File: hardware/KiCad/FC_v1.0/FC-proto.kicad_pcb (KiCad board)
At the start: 4 copper layers, 56 x 46 mm, 134 parts, among them J1 SM06B-GHS-TB, J10 PAD_OUT, J11 PAD_OUT, J12 PAD_OUT_Mini, J13 PAD_OUT_Mini, J2 MEM2061-01-188-00-A, J3 USB4105-GF-A, J4 Conn_ARM_SWD_TagConnect_TC203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, J5 SM06B-GHS-TB, J6 SM04B-GHS-TB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

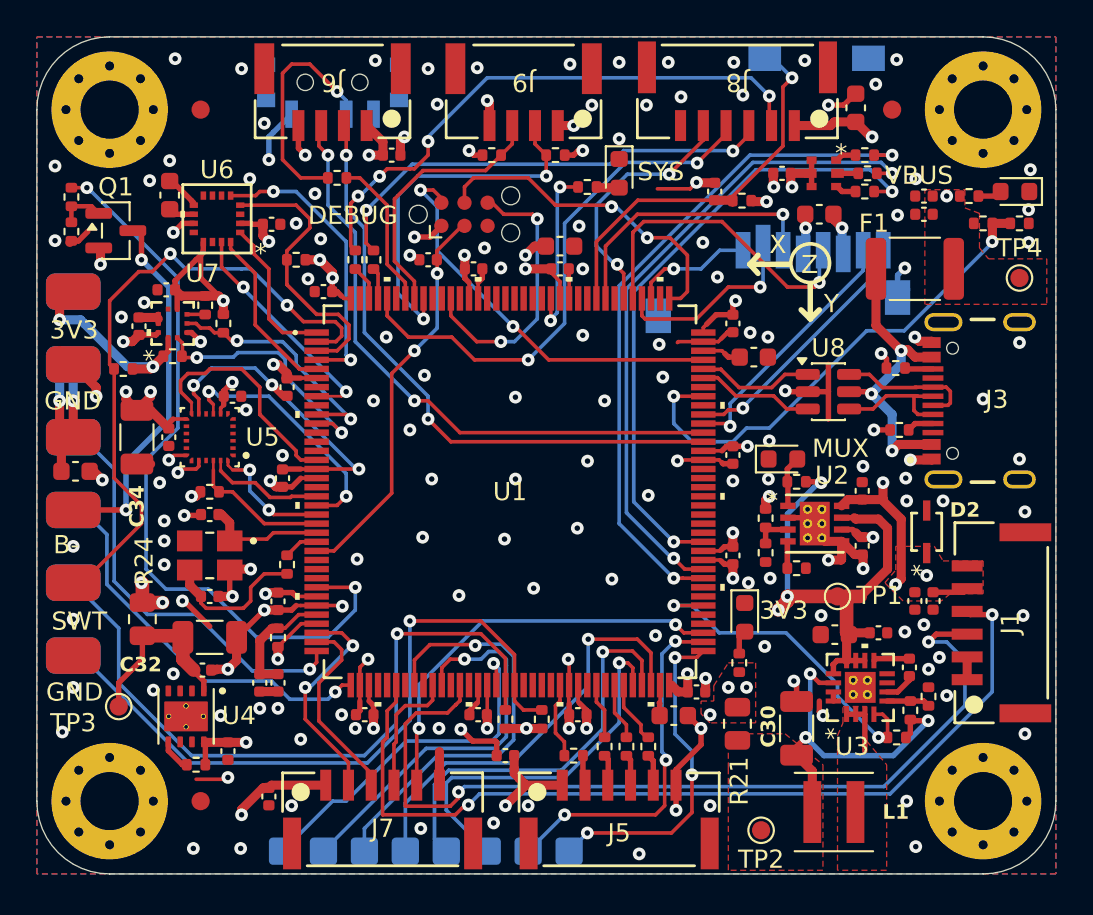
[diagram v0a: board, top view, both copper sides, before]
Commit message: changing USB ESD IC (v0.8)
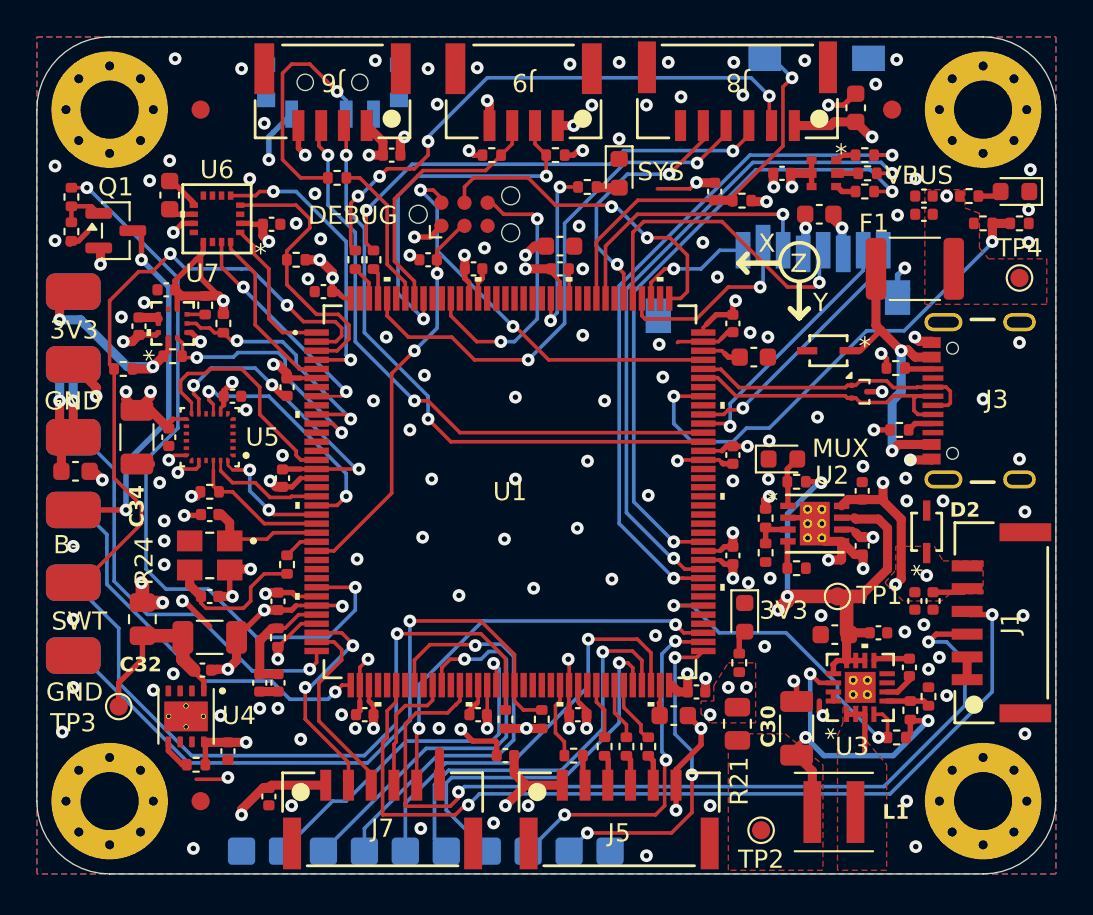
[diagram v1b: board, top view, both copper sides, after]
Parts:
- added D5: TSD05DYFR, FC-FootprintLib:TVS_SOD2_DYF_TEX, F.Cu at (113.5, 94.2)
- J12, J13: footprint FC-FootprintLib:Pad_out_mini_1x4 -> FC-FootprintLib:Pad_out_mini_1x5
- R27, R28: value 4.7k -> 2.2k
- U8: value USBLC6-2SC6 -> TPD2EUSB30A; footprint Package_TO_SOT_SMD:SOT-23-6 -> Package_TO_SOT_SMD:Texas_DRT-3
- moved J12 2.25 mm to (102.2, 121.0)
- moved U8 1.70 mm to (115.2, 96.5), turned to -90 degrees
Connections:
- F1 pad 1: Net-(U8-VBUS) -> Net-(D5-K)
- J12 pad 1: UART5_RX -> GND
- J12 pad 2: UART5_TX -> UART5_RX
- J12 pad 3: GPIO_68 -> UART5_TX
- J12 pad 4: GPIO_69 -> GPIO_68
- J3 pad A4: Net-(U8-VBUS) -> Net-(D5-K)
- J3 pad B4: Net-(U8-VBUS) -> Net-(D5-K)
- U8 pad 2: GND -> USB_D-
- U8 pad 3: USB_D- -> GND
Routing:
- net Net-(U8-VBUS): track 17.3 -> 0.00 mm, vias 3 -> 0
- net Net-(D5-K): track 0.00 -> 17.2 mm, vias 0 -> 2
- net GND: track 125.6 -> 121.1 mm
- net USB_D-: track 13.3 -> 16.3 mm
- net USB_D+: track 14.2 -> 16.1 mm
- net +5V: track 51.0 -> 51.5 mm
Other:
- board text added: "// FC Dev Board // v0.8 // G.A, S.B"
- board text removed: "// FC Dev Board // v0.7 // G.A, S.B"

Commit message: Component library update
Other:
- board text added: "D5"
- board text added: "U8"
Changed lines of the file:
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@@
 		(grid_origin 70 123)
 		(pcbplotparams
-			(layerselection 0x00000000_00000000_55555555_5755f5ff)
+			(layerselection 0x00000000_00000000_55555555_5755f5fb)
 			(plot_on_all_layers_selection 0x00000000_00000000_00000000_00000000)
 			(disableapertmacros no)
@@
 			(usegerberattributes yes)
 			(usegerberadvancedattributes yes)
-			(creategerberjobfile yes)
+			(creategerberjobfile no)
 			(dashed_line_dash_ratio 12.000000)
 			(dashed_line_gap_ratio 3.000000)
@@
 			(plotframeref no)
 			(mode 1)
-			(useauxorigin no)
+			(useauxorigin yes)
 			(hpglpennumber 1)
 			(hpglpenspeed 20)
@@
 			(outputformat 1)
 			(mirror no)
-			(drillshape 1)
+			(drillshape 0)
 			(scaleselection 1)
-			(outputdirectory "")
+			(outputdirectory "../../../exports/manufacturing/")
 		)
 	)
@@
 		(tags "BMP390 ")
 		(property "Reference" "U7"
-			(at 2.750001 1.6374 0)
+			(at -2.049999 2.7374 0)
 			(unlocked yes)
 			(layer "F.SilkS")
@@
 		(tags "MMC5983MA ")
 		(property "Reference" "U6"
-			(at 0 2.7 0)
+			(at 0 2.8 0)
 			(unlocked yes)
 			(layer "F.SilkS")
@@
 			(net 2 "+3.3V")
 			(pintype "passive")
-			(teardrops
-				(best_length_ratio 0.5)
-				(max_length 1)
-				(best_width_ratio 1)
-				(max_width 2)
-				(curved_edges no)
-				(filter_ratio 0.9)
-				(enabled yes)
-				(allow_two_segments yes)
-				(prefer_zone_connections yes)
-			)
 		)
 		(pad "2" smd roundrect
@@
 			(net 1 "GND")
 			(pintype "passive")
-			(zone_connect 2)
 		)
 		(embedded_fonts no)
@@
 		(layer "Edge.Cuts")
 	)
+	(gr_text "U8\n"
+		(at 113.2 97.8 0)
+		(layer "F.SilkS")
+		(effects
+			(font
+				(size 1 1)
+				(thickness 0.15)
+			)
+		)
+	)
 	(gr_text "3V3"
 		(at 70.7 93.7 0)
@@
 		)
 	)
+	(gr_text "D5"
+		(at 113 96.2 0)
+		(layer "F.SilkS")
+		(effects
+			(font
+				(size 0.8 0.8)
+				(thickness 0.16)
+				(bold yes)
+			)
+		)
+	)
 	(gr_text "TX"
 		(at 73 101.6 0)
@@
 	)
 	(zone
-		(net 2)
-		(net_name "+3.3V")
-		(layer "F.Cu")
-		(name "$teardrop_padvia$")
-		(hatch none 0.1)
-		(priority 30001)
-		(attr
-			(teardrop
-				(type padvia)
-			)
-		)
-		(connect_pads yes
-			(clearance 0)
-		)
-		(min_thickness 0.0254)
-		(filled_areas_thickness no)
-		(fill yes
-			(thermal_gap 0.5)
-			(thermal_bridge_width 0.5)
-			(island_removal_mode 1)
-			(island_area_min 10)
-		)
-		(polygon
-			(pts
-				(xy 93.77 89.16) (xy 93.27 89.16) (xy 93.24 89.58) (xy 93.52 89.751) (xy 93.8 89.58)
-			)
-		)
-	)
-	(zone
 		(net 0)
 		(net_name "")
@@
 			)
 		)
-	)
-	(zone
-		(net 2)
-		(net_name "+3.3V")
-		(layer "F.Cu")
-		(name "$teardrop_padvia$")
-		(hatch none 0.1)
-		(priority 30016)
-		(attr
-			(teardrop
-				(type padvia)
-			)
-		)
-		(connect_pads yes
-			(clearance 0)
-		)
-		(min_thickness 0.0254)
-		(filled_areas_thickness no)
-		(fill yes
-			(thermal_gap 0.5)
-			(thermal_bridge_width 0.5)
-			(island_removal_mode 1)
-			(island_area_min 10)
-		)
-		(polygon
-			(pts
-				(xy 93.463432 90.425563) (xy 93.675563 90.213432) (xy 93.789343 89.973576) (xy 93.519293 89.749293)
-				(xy 93.259065 89.986159)
-			)
-		)

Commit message: manufacturing exports v0.9
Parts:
- D2, D5: value TSD05DYFR -> LTVS16H5; footprint FC-FootprintLib:TVS_SOD2_DYF_TEX -> FC-FootprintLib:DFN1610-2
- F1: footprint Resistor_SMD:R_1812_4532Metric -> Fuse:Fuse_1812_4532Metric
- J12, J13: value PAD_OUT_Mini -> Conn_01x05
- Q1: footprint Package_TO_SOT_SMD:SOT-23 -> Package_TO_SOT_SMD:SOT-23-3
- TP1, TP2, TP3, TP4: value TestPoint Pad -> TestPoint
- Y2: footprint FC-FootprintLib:TSX-3225_16MHz -> Crystal:Crystal_SMD_2520-4Pin_2.5x2.0mm
- moved D5 2.41 mm to (115.5, 92.9)
- moved Q1 0.43 mm to (74.5, 87.2)
- moved D2 0.34 mm to (118.8, 104.5)
- moved L1 0.20 mm to (113.8, 119.8), turned to 180 degrees
- moved F1 0.07 mm to (118.2, 89.8), turned to 180 degrees
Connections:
- F1 pad 1: Net-(D5-K) -> VBUS
- F1 pad 2: VBUS -> Net-(D5-K)
- L1 pad 1: /Power Section/Buck_Out -> /Power Section/SW_L
- L1 pad 2: /Power Section/SW_L -> /Power Section/Buck_Out
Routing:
- net GND: track 121.1 -> 118.7 mm, vias 161 -> 160
- net Net-(D5-K): track 17.2 -> 15.1 mm
- net HSE_IN: track 6.23 -> 6.94 mm
